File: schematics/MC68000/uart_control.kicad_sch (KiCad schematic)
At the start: 4 parts, among them J11 Conn_02x20_Counter_Clockwise, J12 Conn_02x37_Row_Letter_Last, U28 74LS139, U29 74LS138

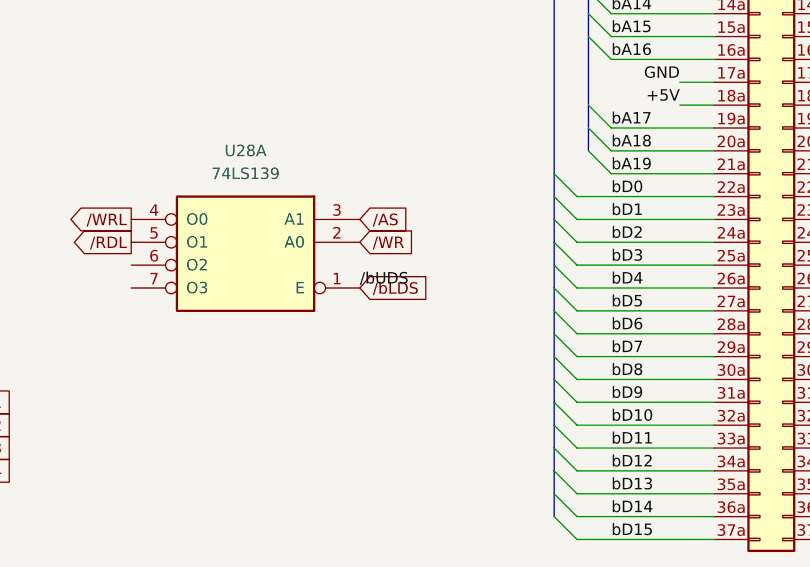
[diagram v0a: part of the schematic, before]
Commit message: Keyboard tested in dir apps/keyboard
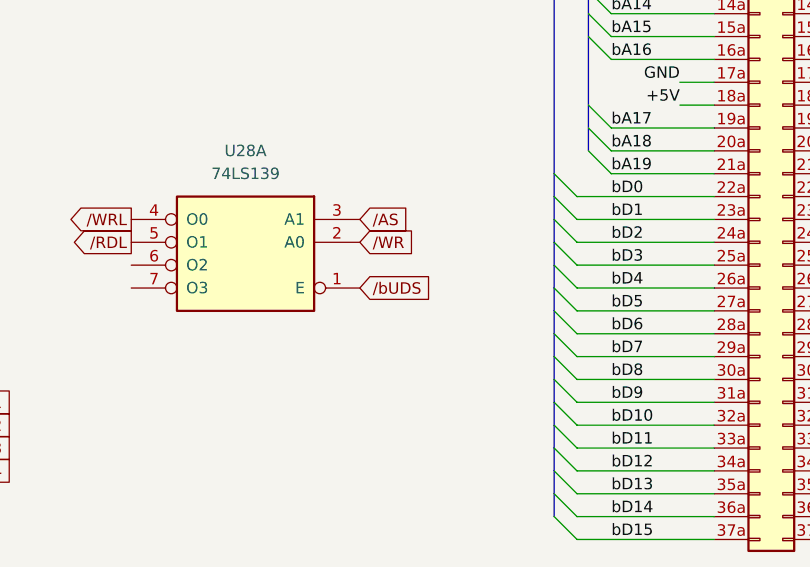
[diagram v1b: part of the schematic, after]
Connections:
- net /bLDS: no longer J12.14b (Pin_14b), U28.1 (E)
- new net /bUDS: J12.14b (Pin_14b), U28.1 (E)
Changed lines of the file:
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@@
-		)
-	)
-	(label "{slash}bUDS"
-		(at 111.76 105.41 0)
-		(effects
-			(font
-				(size 1.27 1.27)
-			)
-			(justify left bottom)
 		)
 	)
@@
 		)
 	)
-	(global_label "{slash}bLDS"
+	(global_label "{slash}bUDS"
 		(shape input)
 		(at 111.76 105.41 0)
@@
 		)
 		(property "Intersheetrefs" "${INTERSHEET_REFS}"
-			(at 120.7323 105.41 0)
-			(effects
-				(font
+			(at 121.0347 105.41 0)
+			(effects
+				(font
